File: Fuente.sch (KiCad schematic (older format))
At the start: 0 parts

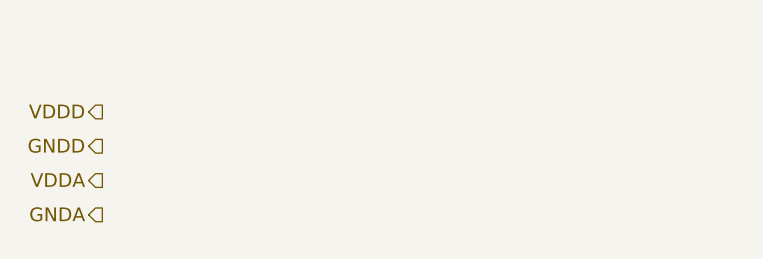
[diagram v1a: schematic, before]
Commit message: Se terminaron todos los simbolos necesarios. Se realizo el esquematico de la fuente y el reloj. Se inicio el esquematico de la parte de señal.
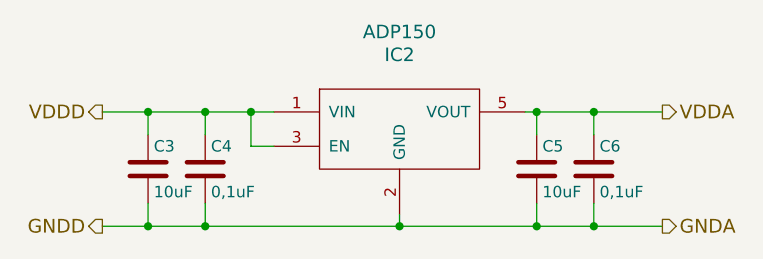
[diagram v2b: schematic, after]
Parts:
- added C3, C5: 10uF, symbol C
- added C4, C6: 0,1uF, symbol C
- added IC2: ADP150, symbol ADP150
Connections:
- net GNDA: now also C3.2, C4.2, C5.2, C6.2, IC2.2 (GND)
- net VDDA: now also C5.1, C6.1, IC2.5 (VOUT)
- net VDDD: now also C3.1, C4.1, IC2.1 (VIN), IC2.3 (EN)
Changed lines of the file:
@@
 LIBS:contrib
 LIBS:valves
+LIBS:PMOD_IA
 LIBS:proyectoDCI-cache
 EELAYER 25 0
@@
 Text HLabel 5050 2650 0    60   Output ~ 0
 VDDD
-Text HLabel 5050 2800 0    60   Output ~ 0
+Text HLabel 5050 3150 0    60   Output ~ 0
 GNDD
-Text HLabel 5050 2950 0    60   Output ~ 0
+Text HLabel 7500 2650 2    60   Output ~ 0
 VDDA
-Text HLabel 5050 3100 0    60   Output ~ 0
+Text HLabel 7500 3150 2    60   Output ~ 0
 GNDA
+$Comp
+L ADP150 IC2
+U 1 1 582F5A80
+P 6350 2700
+F 0 "IC2" H 6350 3000 59  0000 C CNN
+F 1 "ADP150" H 6350 3100 59  0000 C CNN
+F 2 "" H 6350 2700 59  0001 C CNN
+F 3 "" H 6350 2700 59  0001 C CNN
+	1    6350 2700
+	1    0    0    -1
+$EndComp
+Wire Wire Line
+	5800 2650 5700 2650
+Wire Wire Line
+	5700 2650 5500 2650
+Wire Wire Line
+	5500 2650 5250 2650
+Wire Wire Line
+	5250 2650 5050 2650
+Wire Wire Line
+	5800 2800 5700 2800
+Wire Wire Line
+	5700 2800 5700 2650
+Connection ~ 5700 2650
+Wire Wire Line
+	6900 2650 6950 2650
+Wire Wire Line
+	6950 2650 7200 2650
+Wire Wire Line
+	7200 2650 7500 2650
+$Comp
+L C C3
+U 1 1 582F5B1F
+P 5250 2900
+F 0 "C3" H 5275 3000 50  0000 L CNN
+F 1 "10uF" H 5275 2800 50  0000 L CNN
+F 2 "" H 5288 2750 50  0000 C CNN
+F 3 "" H 5250 2900 50  0000 C CNN
+	1    5250 2900
+	1    0    0    -1
+$EndComp
+$Comp
+L C C4
+U 1 1 582F5B72
+P 5500 2900
+F 0 "C4" H 5525 3000 50  0000 L CNN
+F 1 "0,1uF" H 5525 2800 50  0000 L CNN
+F 2 "" H 5538 2750 50  0000 C CNN
+F 3 "" H 5500 2900 50  0000 C CNN
+	1    5500 2900
+	1    0    0    -1
+$EndComp
+$Comp
+L C C5
+U 1 1 582F5BCF
+P 6950 2900
+F 0 "C5" H 6975 3000 50  0000 L CNN
+F 1 "10uF" H 6975 2800 50  0000 L CNN
+F 2 "" H 6988 2750 50  0000 C CNN
+F 3 "" H 6950 2900 50  0000 C CNN
+	1    6950 2900
+	1    0    0    -1
+$EndComp
+$Comp
+L C C6
+U 1 1 582F5C15
+P 7200 2900
+F 0 "C6" H 7225 3000 50  0000 L CNN
+F 1 "0,1uF" H 7225 2800 50  0000 L CNN
+F 2 "" H 7238 2750 50  0000 C CNN
+F 3 "" H 7200 2900 50  0000 C CNN
+	1    7200 2900
+	1    0    0    -1
+$EndComp
+Wire Wire Line
+	5250 2750 5250 2650
+Connection ~ 5250 2650
+Wire Wire Line
+	5500 2750 5500 2650
+Connection ~ 5500 2650
+Wire Wire Line
+	7500 3150 7200 3150
+Wire Wire Line
+	7200 3150 6950 3150
+Wire Wire Line
+	6950 3150 6350 3150
+Wire Wire Line
+	6350 3150 5500 3150
+Wire Wire Line
+	5500 3150 5250 3150
+Wire Wire Line
+	5250 3150 5050 3150
+Wire Wire Line
+	6350 3100 6350 3150
+Connection ~ 6350 3150
+Wire Wire Line
+	5250 3050 5250 3150
+Connection ~ 5250 3150
+Wire Wire Line
+	5500 3050 5500 3150
+Connection ~ 5500 3150
+Wire Wire Line
+	6950 3050 6950 3150
+Connection ~ 6950 3150
+Wire Wire Line
+	7200 3050 7200 3150
+Connection ~ 7200 3150
+Wire Wire Line
+	7200 2750 7200 2650
+Connection ~ 7200 2650
+Wire Wire Line
+	6950 2750 6950 2650
+Connection ~ 6950 2650
 $EndSCHEMATC

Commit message: Se trabajo sobre la hoja de señal. Se terminó el esquemático, salvo que resta agregar los conectores.
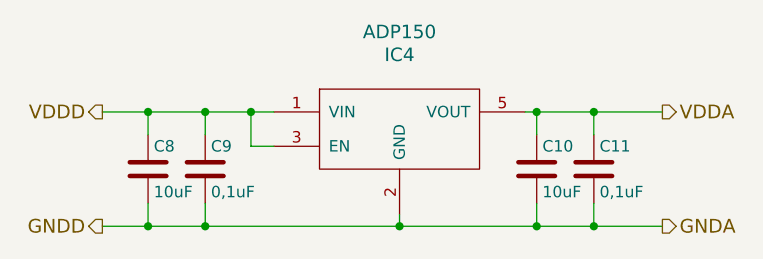
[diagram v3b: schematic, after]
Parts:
- renumbered C5 to C10, C6 to C11, C3 to C8, C4 to C9, IC2 to IC4
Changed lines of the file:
@@
 LIBS:valves
 LIBS:PMOD_IA
+LIBS:SMA
 LIBS:proyectoDCI-cache
 EELAYER 25 0
@@
 GNDA
 $Comp
-L ADP150 IC2
+L ADP150 IC4
 U 1 1 582F5A80
 P 6350 2700
-F 0 "IC2" H 6350 3000 59  0000 C CNN
+F 0 "IC4" H 6350 3000 59  0000 C CNN
 F 1 "ADP150" H 6350 3100 59  0000 C CNN
 F 2 "" H 6350 2700 59  0001 C CNN
@@
 	7200 2650 7500 2650
 $Comp
-L C C3
+L C C8
 U 1 1 582F5B1F
 P 5250 2900
-F 0 "C3" H 5275 3000 50  0000 L CNN
+F 0 "C8" H 5275 3000 50  0000 L CNN
 F 1 "10uF" H 5275 2800 50  0000 L CNN
 F 2 "" H 5288 2750 50  0000 C CNN
@@
 $EndComp
 $Comp
-L C C4
+L C C9
 U 1 1 582F5B72
 P 5500 2900
-F 0 "C4" H 5525 3000 50  0000 L CNN
+F 0 "C9" H 5525 3000 50  0000 L CNN
 F 1 "0,1uF" H 5525 2800 50  0000 L CNN
 F 2 "" H 5538 2750 50  0000 C CNN
@@
 $EndComp
 $Comp
-L C C5
+L C C10
 U 1 1 582F5BCF
 P 6950 2900
-F 0 "C5" H 6975 3000 50  0000 L CNN
+F 0 "C10" H 6975 3000 50  0000 L CNN
 F 1 "10uF" H 6975 2800 50  0000 L CNN
 F 2 "" H 6988 2750 50  0000 C CNN
@@
 $EndComp
 $Comp
-L C C6
+L C C11
 U 1 1 582F5C15
 P 7200 2900
-F 0 "C6" H 7225 3000 50  0000 L CNN
+F 0 "C11" H 7225 3000 50  0000 L CNN
 F 1 "0,1uF" H 7225 2800 50  0000 L CNN
 F 2 "" H 7238 2750 50  0000 C CNN

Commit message: Agregados los conectores. Finalizado el esquemático
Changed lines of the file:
@@
 $EndComp
 Wire Wire Line
-	5800 2650 5700 2650
-Wire Wire Line
-	5700 2650 5500 2650
-Wire Wire Line
-	5500 2650 5250 2650
-Wire Wire Line
-	5250 2650 5050 2650
+	5050 2650 5800 2650
 Wire Wire Line
 	5800 2800 5700 2800
@@
 Connection ~ 5700 2650
 Wire Wire Line
-	6900 2650 6950 2650
-Wire Wire Line
-	6950 2650 7200 2650
-Wire Wire Line
-	7200 2650 7500 2650
+	6900 2650 7500 2650
 $Comp
 L C C8
@@
 Connection ~ 5500 2650
 Wire Wire Line
-	7500 3150 7200 3150
-Wire Wire Line
-	7200 3150 6950 3150
-Wire Wire Line
-	6950 3150 6350 3150
-Wire Wire Line
-	6350 3150 5500 3150
-Wire Wire Line
-	5500 3150 5250 3150
-Wire Wire Line
-	5250 3150 5050 3150
+	5050 3150 7500 3150
 Wire Wire Line
 	6350 3100 6350 3150

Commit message: Footprints creados y linkeados. Listo para proceder al PCB. Todas las DRC dan OK
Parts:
- C10, C11, C8, C9: footprint (none) -> Capacitors_SMD:C_0805
- IC4: footprint (none) -> TO_SOT_Packages_SMD:SC-70-5
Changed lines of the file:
@@
 LIBS:PMOD_IA
 LIBS:SMA
+LIBS:sma2
 LIBS:proyectoDCI-cache
 EELAYER 25 0
@@
 F 0 "IC4" H 6350 3000 59  0000 C CNN
 F 1 "ADP150" H 6350 3100 59  0000 C CNN
-F 2 "" H 6350 2700 59  0001 C CNN
+F 2 "TO_SOT_Packages_SMD:SC-70-5" H 6350 2700 59  0001 C CNN
 F 3 "" H 6350 2700 59  0001 C CNN
 	1    6350 2700
@@
 F 0 "C8" H 5275 3000 50  0000 L CNN
 F 1 "10uF" H 5275 2800 50  0000 L CNN
-F 2 "" H 5288 2750 50  0000 C CNN
+F 2 "Capacitors_SMD:C_0805" H 5288 2750 50  0001 C CNN
 F 3 "" H 5250 2900 50  0000 C CNN
 	1    5250 2900
@@
 F 0 "C9" H 5525 3000 50  0000 L CNN
 F 1 "0,1uF" H 5525 2800 50  0000 L CNN
-F 2 "" H 5538 2750 50  0000 C CNN
+F 2 "Capacitors_SMD:C_0805" H 5538 2750 50  0001 C CNN
 F 3 "" H 5500 2900 50  0000 C CNN
 	1    5500 2900
@@
 F 0 "C10" H 6975 3000 50  0000 L CNN
 F 1 "10uF" H 6975 2800 50  0000 L CNN
-F 2 "" H 6988 2750 50  0000 C CNN
+F 2 "Capacitors_SMD:C_0805" H 6988 2750 50  0001 C CNN
 F 3 "" H 6950 2900 50  0000 C CNN
 	1    6950 2900
@@
 F 0 "C11" H 7225 3000 50  0000 L CNN
 F 1 "0,1uF" H 7225 2800 50  0000 L CNN
-F 2 "" H 7238 2750 50  0000 C CNN
+F 2 "Capacitors_SMD:C_0805" H 7238 2750 50  0001 C CNN
 F 3 "" H 7200 2900 50  0000 C CNN
 	1    7200 2900

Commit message: Se modificó el esquemático para cumplir con las correcciones propuestas. Resta modificar el rótulo y el símbolo de resistor. Agregar campos KiCost
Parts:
- C10, C11, C8, C9: footprint Capacitors_SMD:C_0805 -> Capacitors_SMD:C_0603
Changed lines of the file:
@@
 encoding utf-8
 Sheet 4 4
-Title ""
-Date ""
-Rev ""
-Comp ""
-Comment1 ""
-Comment2 ""
+Title "Medidor de impedancia (PMOD)"
+Date "2016-11-17"
+Rev "A"
+Comp "CESE - FIUBA"
+Comment1 "Autor: LAROSA, F."
+Comment2 "Revisor: GIGLIOTTI, E."
 Comment3 ""
 Comment4 ""
@@
 F 0 "C8" H 5275 3000 50  0000 L CNN
 F 1 "10uF" H 5275 2800 50  0000 L CNN
-F 2 "Capacitors_SMD:C_0805" H 5288 2750 50  0001 C CNN
+F 2 "Capacitors_SMD:C_0603" H 5288 2750 50  0001 C CNN
 F 3 "" H 5250 2900 50  0000 C CNN
 	1    5250 2900
@@
 F 0 "C9" H 5525 3000 50  0000 L CNN
 F 1 "0,1uF" H 5525 2800 50  0000 L CNN
-F 2 "Capacitors_SMD:C_0805" H 5538 2750 50  0001 C CNN
+F 2 "Capacitors_SMD:C_0603" H 5538 2750 50  0001 C CNN
 F 3 "" H 5500 2900 50  0000 C CNN
 	1    5500 2900
@@
 F 0 "C10" H 6975 3000 50  0000 L CNN
 F 1 "10uF" H 6975 2800 50  0000 L CNN
-F 2 "Capacitors_SMD:C_0805" H 6988 2750 50  0001 C CNN
+F 2 "Capacitors_SMD:C_0603" H 6988 2750 50  0001 C CNN
 F 3 "" H 6950 2900 50  0000 C CNN
 	1    6950 2900
@@
 F 0 "C11" H 7225 3000 50  0000 L CNN
 F 1 "0,1uF" H 7225 2800 50  0000 L CNN
-F 2 "Capacitors_SMD:C_0805" H 7238 2750 50  0001 C CNN
+F 2 "Capacitors_SMD:C_0603" H 7238 2750 50  0001 C CNN
 F 3 "" H 7200 2900 50  0000 C CNN
 	1    7200 2900

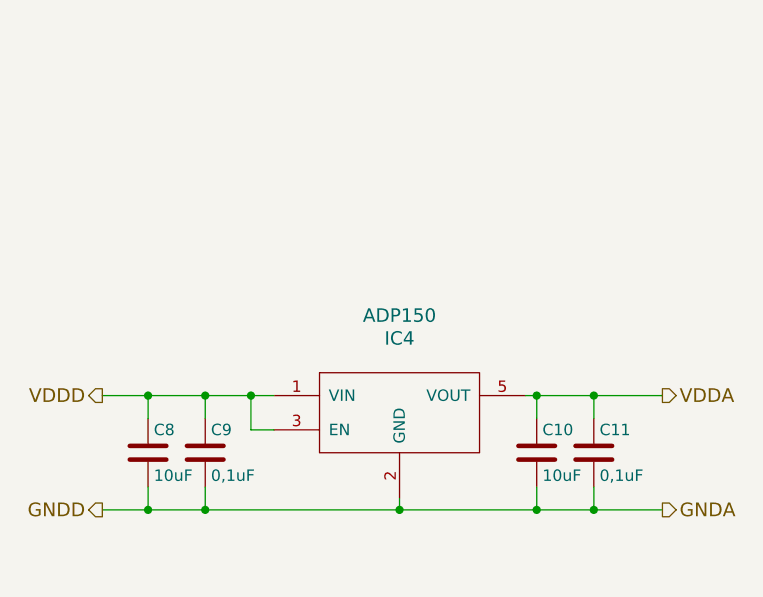
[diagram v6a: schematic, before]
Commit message: Reformulado el esquematico para contener el diseño en dos hojas
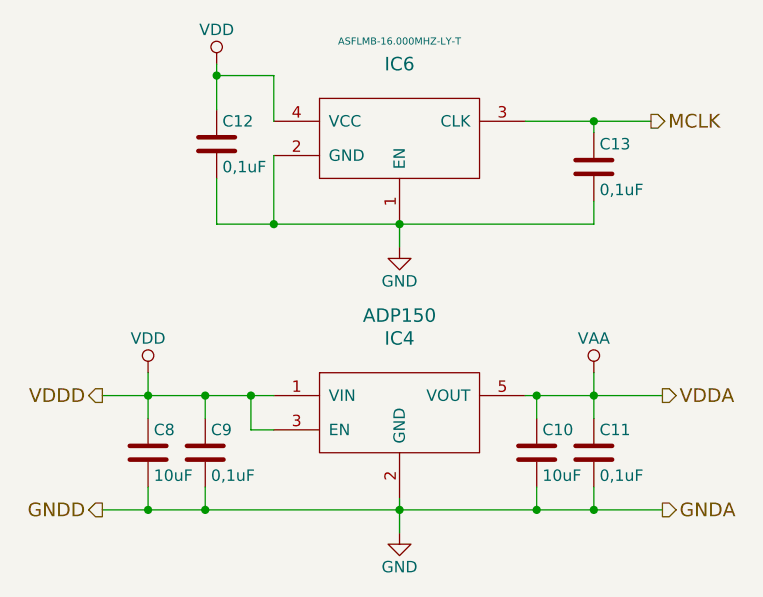
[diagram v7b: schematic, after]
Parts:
- added C12, C13: 0,1uF, Capacitors_SMD:C_0603, symbol C
- added IC6: ASFLMB-16.000MHZ-LY-T, propios:TCXO, symbol ASFLMB-16.000MHZ-LY-T
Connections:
- net GNDA renamed GND
- net GND: now also C12.2, C13.2, IC6.1 (EN), IC6.2 (GND)
- net VDDA renamed VAA
- net VDDD renamed VDD
- net VDD: now also C12.1, IC6.4 (VCC)
- new net MCLK: C13.1, IC6.3 (CLK)
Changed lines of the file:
@@
 $Descr A4 11693 8268
 encoding utf-8
-Sheet 4 4
+Sheet 3 3
 Title "Medidor de impedancia (PMOD)"
 Date "2016-11-17"
@@
 $EndComp
 Wire Wire Line
-	5250 2750 5250 2650
+	5250 2550 5250 2750
 Connection ~ 5250 2650
 Wire Wire Line
@@
 	5050 3150 7500 3150
 Wire Wire Line
-	6350 3100 6350 3150
+	6350 3100 6350 3250
 Connection ~ 6350 3150
 Wire Wire Line
@@
 Connection ~ 7200 3150
 Wire Wire Line
-	7200 2750 7200 2650
+	7200 2550 7200 2750
 Connection ~ 7200 2650
 Wire Wire Line
 	6950 2750 6950 2650
 Connection ~ 6950 2650
+Text HLabel 7450 1450 2    60   Output ~ 0
+MCLK
+$Comp
+L ASFLMB-16.000MHZ-LY-T IC6
+U 1 1 5838BB55
+P 6350 1500
+F 0 "IC6" H 6350 1800 59  0000 C CNN
+F 1 "ASFLMB-16.000MHZ-LY-T" H 6350 1900 31  0000 C CNN
+F 2 "propios:TCXO" H 6350 1500 59  0001 C CNN
+F 3 "" H 6350 1500 59  0001 C CNN
+	1    6350 1500
+	1    0    0    -1
+$EndComp
+$Comp
+L C C12
+U 1 1 5838BB5C
+P 5550 1550
+F 0 "C12" H 5575 1650 50  0000 L CNN
+F 1 "0,1uF" H 5575 1450 50  0000 L CNN
+F 2 "Capacitors_SMD:C_0603" H 5588 1400 50  0001 C CNN
+F 3 "" H 5550 1550 50  0000 C CNN
+	1    5550 1550
+	1    0    0    -1
+$EndComp
+$Comp
+L C C13
+U 1 1 5838BB63
+P 7200 1650
+F 0 "C13" H 7225 1750 50  0000 L CNN
+F 1 "0,1uF" H 7225 1550 50  0000 L CNN
+F 2 "Capacitors_SMD:C_0603" H 7238 1500 50  0001 C CNN
+F 3 "" H 7200 1650 50  0000 C CNN
+	1    7200 1650
+	1    0    0    -1
+$EndComp
+Wire Wire Line
+	5550 1250 5800 1250
+Wire Wire Line
+	5800 1250 5800 1450
+Wire Wire Line
+	5550 1900 7200 1900
+Wire Wire Line
+	5800 1900 5800 1600
+Wire Wire Line
+	5550 1900 5550 1700
+Wire Wire Line
+	5550 1200 5550 1400
+Connection ~ 5800 1900
+Wire Wire Line
+	6900 1450 7450 1450
+Wire Wire Line
+	7200 1500 7200 1450
+Connection ~ 7200 1450
+Wire Wire Line
+	7200 1900 7200 1800
+Connection ~ 6350 1900
+$Comp
+L VDD #PWR025
+U 1 1 5838BBAA
+P 5250 2550
+F 0 "#PWR025" H 5250 2400 50  0001 C CNN
+F 1 "VDD" H 5250 2700 50  0000 C CNN
+F 2 "" H 5250 2550 50  0000 C CNN
+F 3 "" H 5250 2550 50  0000 C CNN
+	1    5250 2550
+	1    0    0    -1
+$EndComp
+$Comp
+L VAA #PWR026
+U 1 1 5838BBE6
+P 7200 2550
+F 0 "#PWR026" H 7200 2400 50  0001 C CNN
+F 1 "VAA" H 7200 2700 50  0000 C CNN
+F 2 "" H 7200 2550 50  0000 C CNN
+F 3 "" H 7200 2550 50  0000 C CNN
+	1    7200 2550
+	1    0    0    -1
+$EndComp
+$Comp
+L VDD #PWR027
+U 1 1 5838BD6B
+P 5550 1200
+F 0 "#PWR027" H 5550 1050 50  0001 C CNN
+F 1 "VDD" H 5550 1350 50  0000 C CNN
+F 2 "" H 5550 1200 50  0000 C CNN
+F 3 "" H 5550 1200 50  0000 C CNN
+	1    5550 1200
+	1    0    0    -1
+$EndComp
+Connection ~ 5550 1250
+$Comp
+L GND #PWR028
+U 1 1 5838BDFD
+P 6350 3250
+F 0 "#PWR028" H 6350 3000 50  0001 C CNN
+F 1 "GND" H 6350 3100 50  0000 C CNN
+F 2 "" H 6350 3250 50  0000 C CNN
+F 3 "" H 6350 3250 50  0000 C CNN
+	1    6350 3250
+	1    0    0    -1
+$EndComp
+$Comp
+L GND #PWR029
+U 1 1 5838BE21
+P 6350 2000
+F 0 "#PWR029" H 6350 1750 50  0001 C CNN
+F 1 "GND" H 6350 1850 50  0000 C CNN
+F 2 "" H 6350 2000 50  0000 C CNN
+F 3 "" H 6350 2000 50  0000 C CNN
+	1    6350 2000
+	1    0    0    -1
+$EndComp
+Wire Wire Line
+	6350 2000 6350 1900
 $EndSCHEMATC
